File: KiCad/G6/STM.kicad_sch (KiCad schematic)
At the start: 1 part, among them U16 STM32C011F4U6TR

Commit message: uhhhh im confused gang
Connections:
- net SPI-SDO-MMC: now reaches U16.11 (PA6)
- net SPI-SDI-MMC: now reaches U16.12 (PA7)
- net CS-MMC: now reaches U16.13 (PA8)
- net SPI-SDO-BMI: now reaches U16.14 (PA11(PA9))
- net SPI-SDI-MS5: now reaches U16.15 (PA12(PA10))
- net CS-MS5: now reaches U16.17 (PA14-BOOT0)
- net SPI-SDO-MS5: now reaches U16.18 (PB6)
- net SPI-SDI-BMI: now reaches U16.7 (PA2)
- net CS-BMI: now reaches U16.9 (PA4)
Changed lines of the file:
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@@
 	(generator_version "9.0")
 	(paper "A4")
+	(global_label "SPI-SDO-BMI"
+		(shape input)
+		(at 170.18 86.36 0)
+		(fields_autoplaced yes)
+		(effects
+			(font
+				(size 1.27 1.27)
+			)
+			(justify left)
+		)
+		(property "Intersheetrefs" "${INTERSHEET_REFS}"
+			(at 186.5305 86.36 0)
+			(effects
+				(font
+					(size 1.27 1.27)
+				)
+				(justify left)
+				(hide yes)
+			)
+		)
+	)
+	(global_label "SPI-SDI-BMI"
+		(shape input)
+		(at 119.38 91.44 180)
+		(fields_autoplaced yes)
+		(effects
+			(font
+				(size 1.27 1.27)
+			)
+			(justify right)
+		)
+		(property "Intersheetrefs" "${INTERSHEET_REFS}"
+			(at 103.7552 91.44 0)
+			(effects
+				(font
+					(size 1.27 1.27)
+				)
+				(justify right)
+				(hide yes)
+			)
+		)
+	)
 	(global_label "SPI-SCK-MAIN"
 		(shape input)
@@
 			(effects
 				(font
+					(size 1.27 1.27)
+				)
+				(justify right)
+				(hide yes)
+			)
+		)
+	)
+	(global_label "CS-MMC"
+		(shape input)
+		(at 170.18 83.82 0)
+		(fields_autoplaced yes)
+		(effects
+			(font
+				(size 1.27 1.27)
+			)
+			(justify left)
+		)
+		(property "Intersheetrefs" "${INTERSHEET_REFS}"
+			(at 181.3899 83.82 0)
+			(effects
+				(font
+					(size 1.27 1.27)
+				)
+				(justify left)
+				(hide yes)
+			)
+		)
+	)
+	(global_label "CS-BMI"
+		(shape input)
+		(at 119.38 96.52 180)
+		(fields_autoplaced yes)
+		(effects
+			(font
+				(size 1.27 1.27)
+			)
+			(justify right)
+		)
+		(property "Intersheetrefs" "${INTERSHEET_REFS}"
+			(at 109.0167 96.52 0)
+			(effects
+				(font
+					(size 1.27 1.27)
+				)
+				(justify right)
+				(hide yes)
+			)
+		)
+	)
+	(global_label "SPI-SDI-MMC"
+		(shape input)
+		(at 170.18 81.28 0)
+		(fields_autoplaced yes)
+		(effects
+			(font
+				(size 1.27 1.27)
+			)
+			(justify left)
+		)
+		(property "Intersheetrefs" "${INTERSHEET_REFS}"
+			(at 186.6514 81.28 0)
+			(effects
+				(font
+					(size 1.27 1.27)
+				)
+				(justify left)
+				(hide yes)
+			)
+		)
+	)
+	(global_label "CS-MS5"
+		(shape input)
+		(at 170.18 93.98 0)
+		(fields_autoplaced yes)
+		(effects
+			(font
+				(size 1.27 1.27)
+			)
+			(justify left)
+		)
+		(property "Intersheetrefs" "${INTERSHEET_REFS}"
+			(at 181.0875 93.98 0)
+			(effects
+				(font
+					(size 1.27 1.27)
+				)
+				(justify left)
+				(hide yes)
+			)
+		)
+	)
+	(global_label "SPI-SDI-MS5"
+		(shape input)
+		(at 170.18 88.9 0)
+		(fields_autoplaced yes)
+		(effects
+			(font
+				(size 1.27 1.27)
+			)
+			(justify left)
+		)
+		(property "Intersheetrefs" "${INTERSHEET_REFS}"
+			(at 186.349 88.9 0)
+			(effects
+				(font
+					(size 1.27 1.27)
+				)
+				(justify left)
+				(hide yes)
+			)
+		)
+	)
+	(global_label "SPI-SDO-MS5"
+		(shape input)
+		(at 170.18 99.06 0)
+		(fields_autoplaced yes)
+		(effects
+			(font
+				(size 1.27 1.27)
+			)
+			(justify left)
+		)
+		(property "Intersheetrefs" "${INTERSHEET_REFS}"
+			(at 187.0747 99.06 0)
+			(effects
+				(font
+					(size 1.27 1.27)
+				)
+				(justify left)
+				(hide yes)
+			)
+		)
+	)
+	(global_label "SPI-SDO-MMC"
+		(shape input)
+		(at 119.38 101.6 180)
+		(fields_autoplaced yes)
+		(effects
+			(font
+				(size 1.27 1.27)
+			)
+			(justify right)
+		)
+		(property "Intersheetrefs" "${INTERSHEET_REFS}"
+			(at 102.1829 101.6 0)
+			(effects
+				(font

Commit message: I think the schematics done uhhh idrk
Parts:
- removed U16: STM32C011F4U6TR, STM32C011F4U6TR:IC_STM32C011F4U6TR, symbol STM32C011F4U6TR:STM32C011F4U6TR
- added U1: STM32C051K8T6, CC0603KRXQRQBB104:LQFP32_7x7_STM, symbol STM32C051K8T6:STM32C051K8T6
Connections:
- net CS-BMI: now also U1.1 (PB9)
- net CS-MMC: now also U1.11 (PA4)
- net CS-MS5: now also U1.15 (PB0)
- new net CS-IIM1: U1.25 (PA13-BOOT0)
- new net CS-IIM2: U1.26 (PA15)
- new net CS-TMP: U1.18 (PA8)
- new net MISO-BMI: U1.22 (PA11[PA9])
- new net MOSI-BMI: U1.9 (PA2)
- new net SCK-MAIN: U1.8 (PA1)

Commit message: sasha sneaky academic
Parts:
- renumbered U1 to U12
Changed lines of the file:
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@@
 		(dnp no)
 		(fields_autoplaced yes)
-		(property "Reference" "U1"
+		(property "Reference" "U12"
 			(at 140.97 54.61 0)
 			(effects
@@
 			(project ""
 				(path "/99017594-210d-4d15-87a7-3152ef0d7b7c/dd8d0103-050a-4966-97b1-bf15728af484"
-					(reference "U1")
+					(reference "U12")
 					(unit 1)
 				)

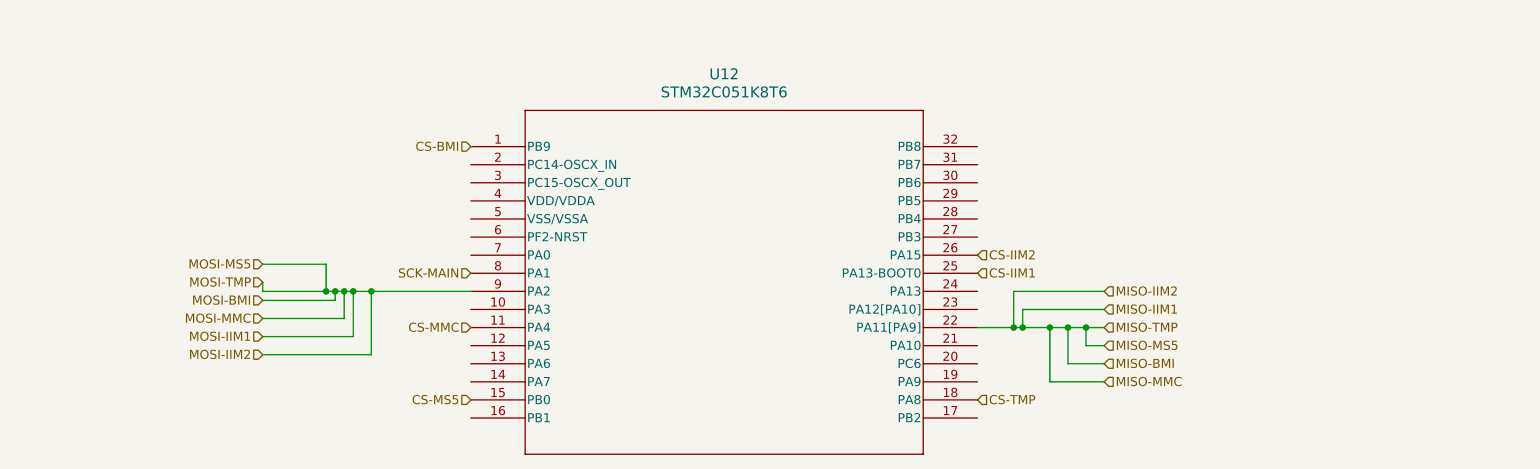
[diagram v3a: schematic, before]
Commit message: errrrrr i cant find a umcx connector they all say there like $50??
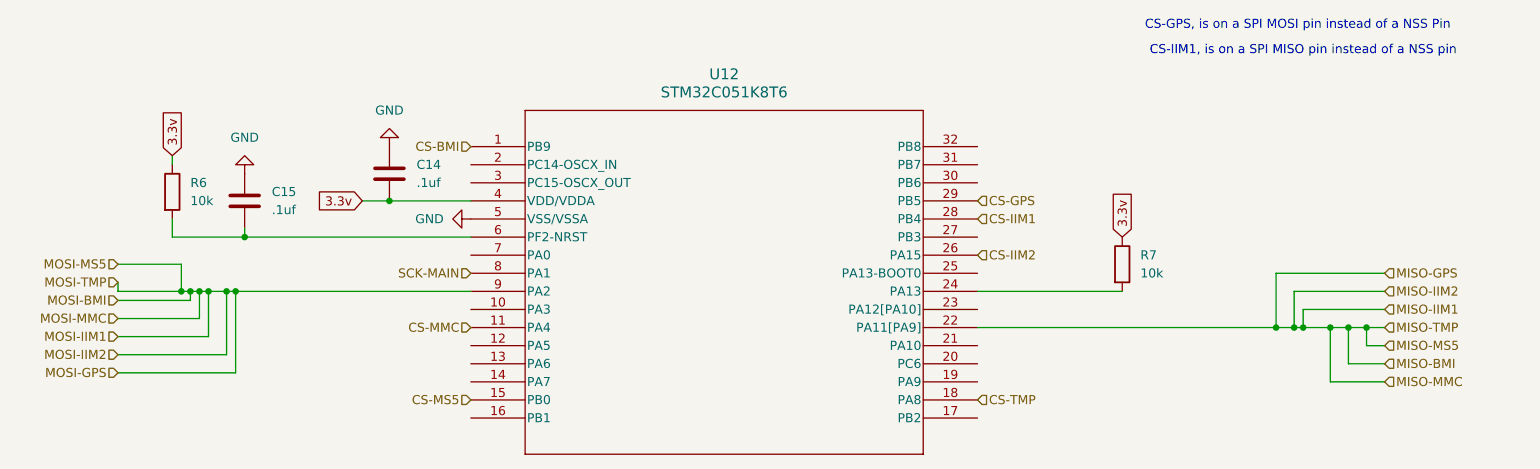
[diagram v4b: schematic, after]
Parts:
- added C14, C15: .1uf, CC0603KRXQRQBB104:.1CAP_CC1206_YAG, symbol Device:C
- added R6, R7: 10k, CC0603KRXQRQBB104:10kRC1206N_YAG, symbol Device:R
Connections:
- net CS-IIM1: now also U12.28 (PB4); no longer U12.25 (PA13-BOOT0)
- net at U12.24 (PA13): now also R7.2
- net CS-GPS: now reaches U12.29 (PB5)
- net 3.3v: now reaches U12.4 (VDD/VDDA)
- net 3.3v: now also C14.2, R6.1, R7.1
- net GND: now reaches U12.5 (VSS/VSSA)
- net GND: now also C14.1, C15.1
- net at U12.6 (PF2-NRST): now also C15.2, R6.2
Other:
- note added: "CS-GPS, is on a SPI MOSI pin instead of a NSS Pin"
- note added: "CS-IIM1, is on a SPI MISO pin instead of a NSS pin"

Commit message: i have no idea whats going on, everything crashed and nothing will open
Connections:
- net TX: now reaches U12.13 (PA6)
- net RX: now reaches U12.14 (PA7)
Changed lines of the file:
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@@
+		)
+	)
+	(hierarchical_label "RX"
+		(shape input)
+		(at 105.41 97.79 180)
+		(effects
+			(font
+				(size 1.27 1.27)
+			)
+			(justify right)
 		)
 	)
@@
 		(effects
 			(font
+				(size 1.27 1.27)
+			)
+			(justify right)
+		)
+	)
+	(hierarchical_label "TX"
+		(shape input)
+		(at 105.41 95.25 180)
+		(effects
+			(font

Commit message: idk whats going on anymore
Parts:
- added C16, C17: 22pf, Capacitor_SMD:C_1206_3216Metric, symbol Device:C
- added Y1: ABS07-32.768KHZ-1-T, CC0603KRXQRQBB104:XTAL_ABS07-32.768KHZ-1-T, symbol ABS07-32.768KHZ-1-T:ABS07-32.768KHZ-1-T
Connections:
- net GND: now also C16.1, C17.1
- net at U12.2 (PC14-OSCX_IN): now also C17.2, Y1.1
- net at U12.3 (PC15-OSCX_OUT): now also C16.2, Y1.2
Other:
- moved on the sheet: C14, C15, R6

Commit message: g6
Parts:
- removed R6, R7: 10k, CC0603KRXQRQBB104:10kRC1206N_YAG, symbol Device:R
- added J3: FTSH-107-01-L-DV-K-A, FTSH_107_01_L_DV_K_A:SAMTEC_FTSH-107-01-L-DV-K-A, symbol FTSH-107-01-L-DV-K-A:FTSH-107-01-L-DV-K-A
- added R4: 100, Resistor_SMD:R_0805_2012Metric, symbol Device:R
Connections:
- net 3.3v: now also J3.03
- net GND: now also J3.05, J3.07, R4.2
- net OSCX_IN: now reaches C16.2, Y1.2
- net OSCX_IN: now also C17.2, U12.2 (PC14-OSCX_IN), Y1.1; no longer U12.3 (PC15-OSCX_OUT)
- net SWDIO: now reaches U12.24 (PA13)
- net SWDIO: now also J3.04
- net SWCLK: now reaches U12.25 (PA13-BOOT0)
- net SWCLK: now also J3.06
- net GPIO: now reaches U12.32 (PB8)
- net NRST: now reaches C15.2, U12.6 (PF2-NRST)
- net NRST: now also J3.12
- new net: J3.11, R4.1
- new net OSCX_OUT: U12.3 (PC15-OSCX_OUT)
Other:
- moved on the sheet: C14, C15, C16, C17, U12, Y1
